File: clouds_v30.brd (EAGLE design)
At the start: 152.4 x 51.1 mm, 148 parts, among them IC1 74HC595D, IC10 TL072D, IC2 LM1117-3.3, IC3 MCP6002, IC4 MCP6004, IC5 STM32F405RGT6, IC6 LM4040B10, IC7 LM1117-3.3, IC8 WM8731, IC9 TL072D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

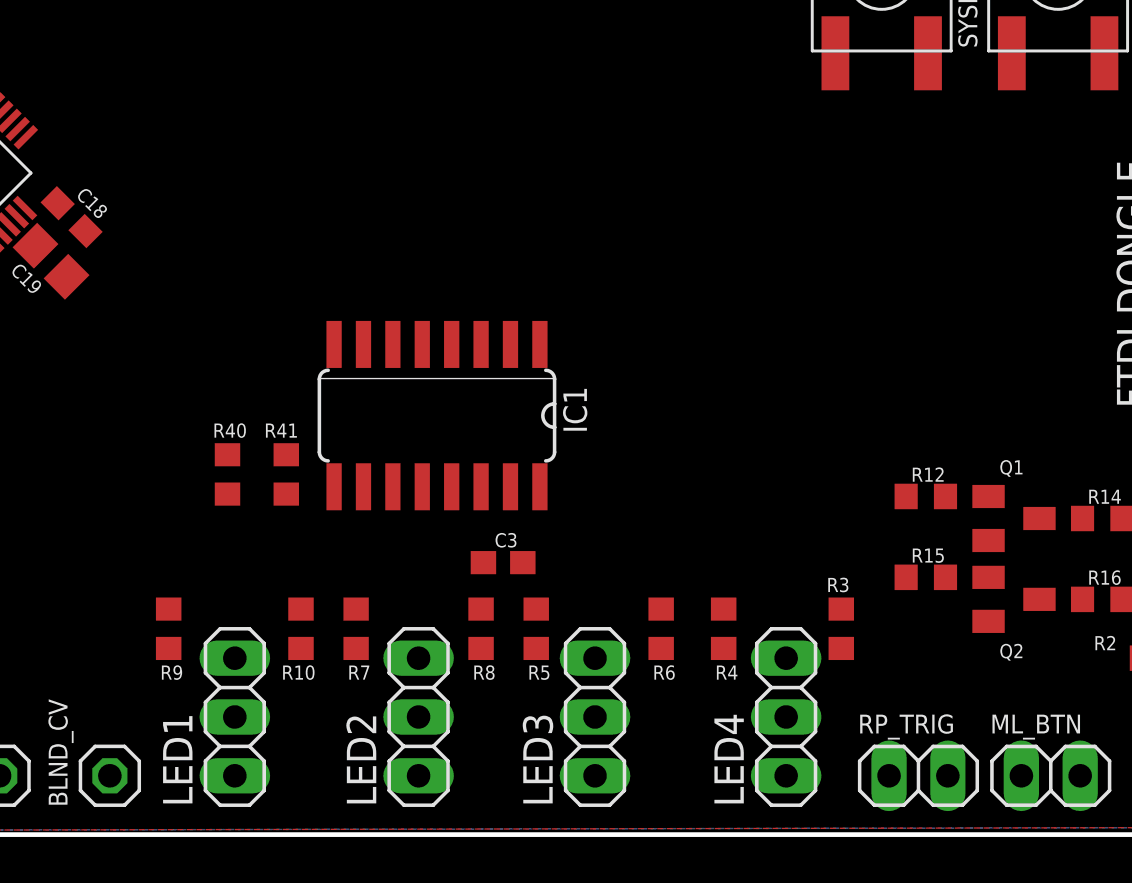
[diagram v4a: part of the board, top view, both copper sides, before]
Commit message: leds mostly routed
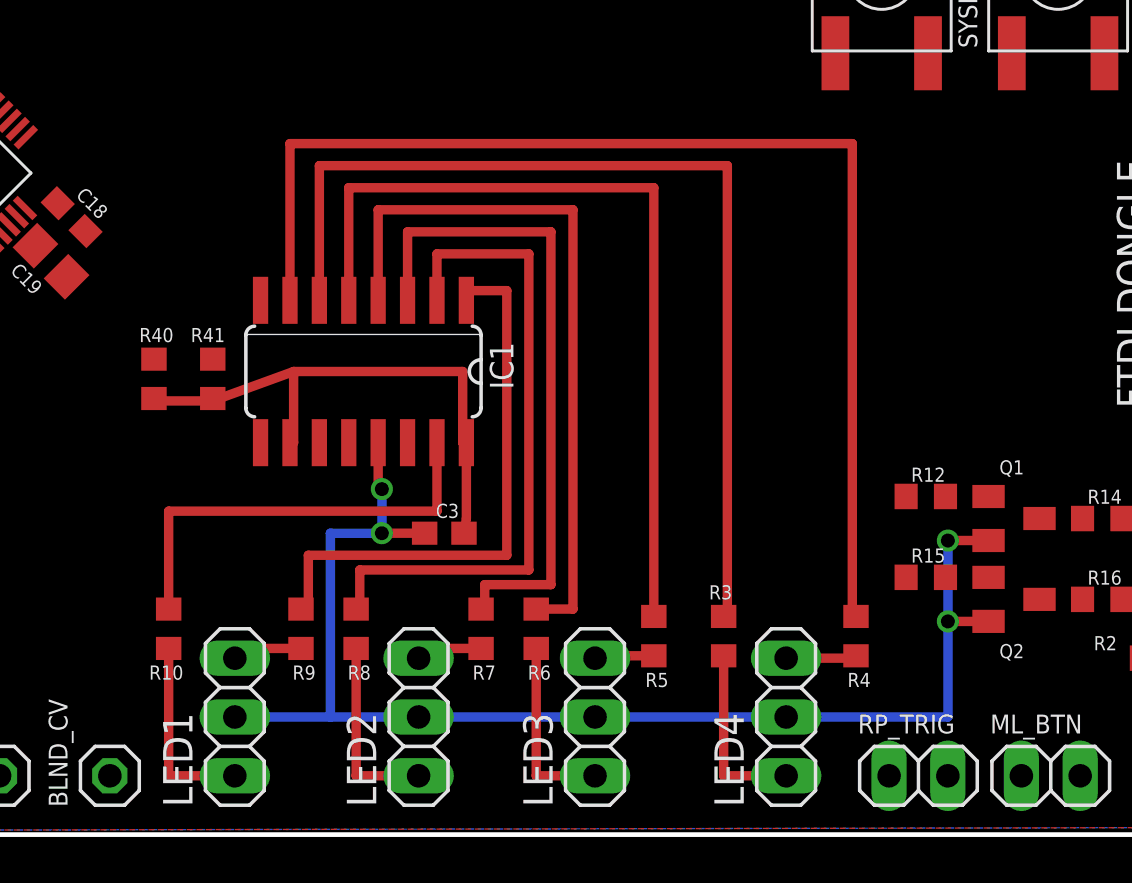
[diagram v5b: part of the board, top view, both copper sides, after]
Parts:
- moved R4 5.72 mm to (131.6, 8.57)
- moved R10 5.71 mm to (101.9, 8.89)
- moved R9 5.71 mm to (107.6, 8.89)
- moved R6 5.40 mm to (117.8, 8.89)
- moved R7 5.40 mm to (115.4, 8.89)
- moved R8 5.40 mm to (110.0, 8.89)
- moved R40 5.21 mm to (101.3, 19.7)
- moved R41 5.21 mm to (103.8, 19.7)
- moved R3 5.09 mm to (125.9, 8.57)
- moved R5 5.09 mm to (122.9, 8.57)
- moved IC1 3.70 mm to (110.3, 20.0)
- moved C3 2.84 mm to (113.8, 13.0)
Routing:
- net GND: track 0.00 -> 58.0 mm, vias 0 -> 4
- net N$50: track 0.00 -> 52.0 mm
- net N$49: track 0.00 -> 43.1 mm
- net N$48: track 0.00 -> 36.6 mm
- net N$47: track 0.00 -> 31.2 mm
- net N$45: track 0.00 -> 28.8 mm
- net N$46: track 0.00 -> 28.5 mm
- net N$44: track 0.00 -> 24.8 mm
- net +3V3: track 0.00 -> 24.1 mm
- net N$43: track 0.00 -> 18.8 mm
- net N$12: track 0.00 -> 8.36 mm
- net N$16: track 0.00 -> 8.20 mm
- net N$34: track 0.00 -> 8.04 mm
- net N$40: track 0.00 -> 7.88 mm
- net N$9: track 0.00 -> 3.28 mm
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
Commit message: more routing!
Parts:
- moved R61 10.8 mm to (16.8, 8.26), turned to 180 degrees
- moved R62 9.53 mm to (27.6, 7.94)
- moved C48 9.42 mm to (30.8, 43.7), turned to 90 degrees
- moved C47 9.42 mm to (30.8, 35.7), turned to 270 degrees
- moved OUT-R 6.98 mm to (24.8, 4.13)
- moved IN-L 4.76 mm to (8.26, 4.13)
- moved IN-R 4.76 mm to (13.0, 4.13)
- moved OUT-L 2.86 mm to (19.7, 4.13)
- moved Q4 1.91 mm to (34.3, 39.7), turned to 90 degrees
- moved C31 1.90 mm to (36.5, 15.9), turned to 90 degrees
- moved IC7 1.42 mm to (36.2, 8.26), turned to 0 degrees
- moved R2 1.27 mm to (146.1, 7.62)
- moved R50 1.00 mm to (47.9, 14.9)
- moved C26 0.95 mm to (48.3, 7.62)
- moved C27 0.95 mm to (43.8, 7.62)
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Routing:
- net GND: track 58.0 -> 252.3 mm
- net +3V3: track 24.1 -> 92.3 mm
- net N$55: track 0.00 -> 24.2 mm
- net N$60: track 0.00 -> 23.7 mm
- net VCC: track 0.00 -> 19.8 mm
- net N$28: track 0.00 -> 19.4 mm
- net +3V3_A: track 0.00 -> 18.8 mm
- net N$33: track 0.00 -> 16.6 mm
- net AREF_-10: track 0.00 -> 13.5 mm
- net N$57: track 0.00 -> 13.4 mm
- net N$59: track 0.00 -> 13.3 mm
- net RESET: track 0.00 -> 11.9 mm
- net BOOT_FLASH: track 0.00 -> 11.9 mm
- net N$21: track 0.00 -> 10.6 mm
- net N$36: track 0.00 -> 10.4 mm
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
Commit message: lots more hand routing
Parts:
- moved R41 23.2 mm to (81.6, 13.0)
- moved R40 23.2 mm to (79.1, 13.0)
- moved C6 9.26 mm to (86.4, 36.8)
- moved C7 8.94 mm to (91.1, 36.8)
- moved Q3 8.94 mm to (89.5, 40.6)
- moved R50 7.63 mm to (48.3, 22.5)
- moved C12 5.43 mm to (80.3, 29.2)
- moved C14 5.43 mm to (81.3, 28.3)
- moved C18 5.43 mm to (97.1, 21.3)
- moved C19 5.43 mm to (96.2, 19.4)
- moved IC5 5.43 mm to (88.3, 23.2)
- moved C17 5.43 mm to (80.0, 21.6)
- moved C24 5.43 mm to (84.1, 15.9)
- moved C8 5.43 mm to (88.3, 31.8)
- moved C25 5.43 mm to (87.3, 14.2)
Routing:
- net +3V3: track 92.3 -> 305.9 mm
- net VCC: track 19.8 -> 83.1 mm
- net +3V3_A: track 18.8 -> 49.0 mm
- net N$26: track 0.00 -> 26.1 mm
- net N$7: track 0.00 -> 22.3 mm
- net AREF_-10: track 13.5 -> 33.3 mm
- net LIN: track 0.00 -> 16.9 mm
- net N$8: track 0.00 -> 14.5 mm
- net RIN: track 0.00 -> 11.5 mm
- net DENSITY_CV: track 0.00 -> 10.3 mm
- net N$30: track 0.00 -> 8.05 mm
- net N$24: track 0.00 -> 7.65 mm
- net N$2: track 0.00 -> 7.29 mm
- net N$5: track 0.00 -> 7.05 mm
- net N$15: track 0.00 -> 6.86 mm
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
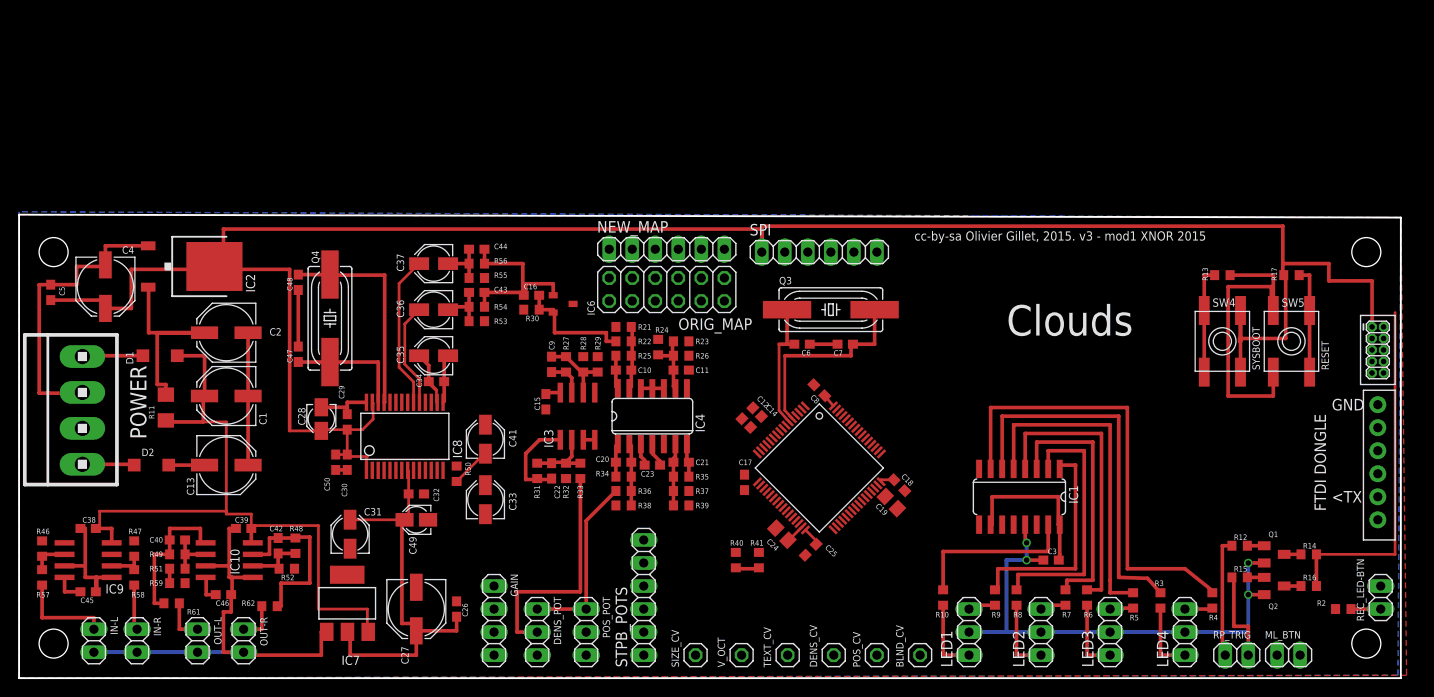
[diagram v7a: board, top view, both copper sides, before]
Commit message: auto routed + some fixup, still some to do
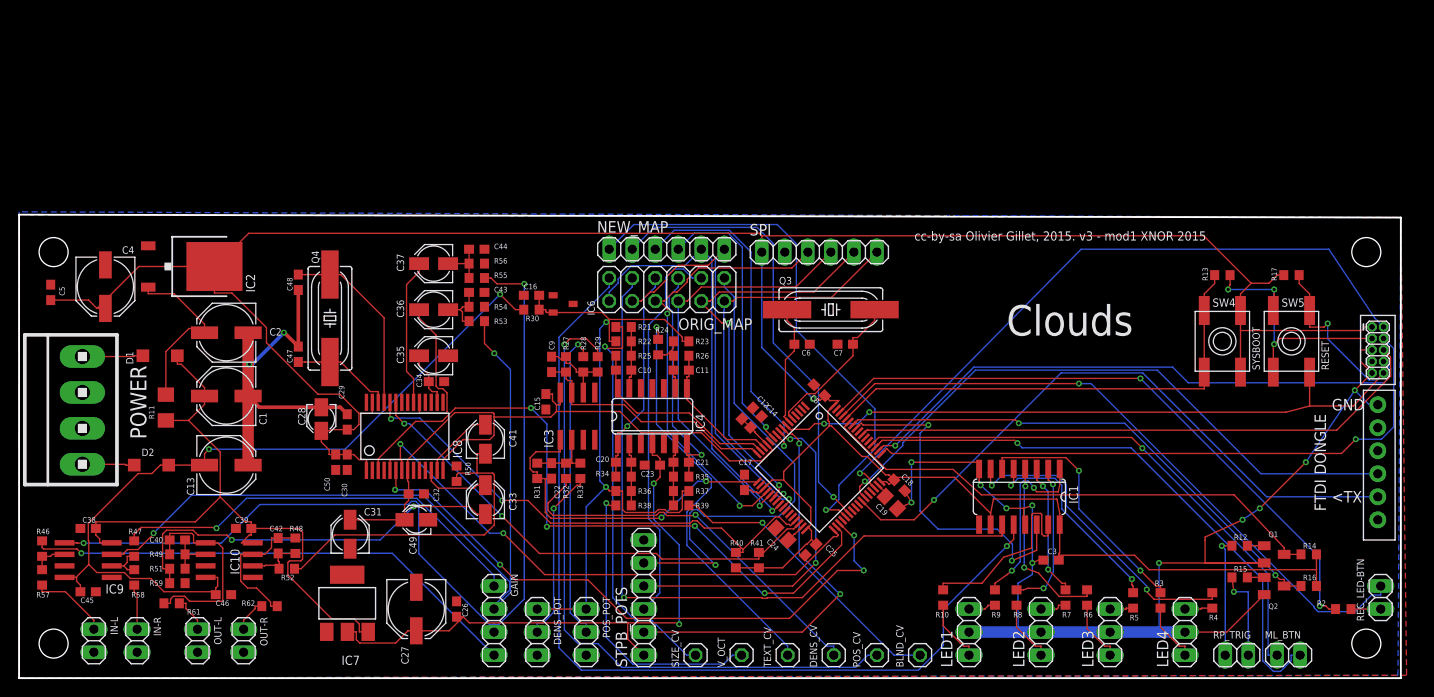
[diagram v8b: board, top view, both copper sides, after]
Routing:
- net LED_EN: track 0.00 -> 104.1 mm, vias 0 -> 1
- net N$51: track 0.00 -> 102.9 mm, vias 0 -> 2
- net +3V3_A: track 49.0 -> 145.4 mm, vias 0 -> 2
- net N$42: track 0.00 -> 88.1 mm, vias 0 -> 2
- net LED_SCK: track 0.00 -> 81.6 mm, vias 0 -> 1
- net RESET: track 11.9 -> 90.8 mm, vias 0 -> 3
- net VEE: track 10.3 -> 88.2 mm, vias 0 -> 2
- net JTMS: track 0.00 -> 75.2 mm, vias 0 -> 1
- net I2S_SCK: track 0.00 -> 74.3 mm, vias 0 -> 4
- net N$27: track 0.00 -> 73.4 mm, vias 0 -> 1
- net SW_REC: track 0.00 -> 73.0 mm, vias 0 -> 1
- net TX: track 0.00 -> 70.1 mm, vias 0 -> 1
- net LED_REC: track 0.00 -> 69.9 mm, vias 0 -> 2
- net RX: track 0.00 -> 68.8 mm, vias 0 -> 1
- net I2S_SIN: track 0.00 -> 68.4 mm, vias 0 -> 4
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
